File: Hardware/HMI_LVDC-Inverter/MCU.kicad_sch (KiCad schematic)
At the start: 44 parts, among them J1 UART, J9 INV, SW10 SW_MEC_5E, SW12 SW_MEC_5E, U3 ESP32-WROOM-32E, Y1 32.768KHz

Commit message: Cambios en los periféricos previo al viaje para poder seguir trabajándolo
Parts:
- renumbered SW12 to SW10, SW10 to SW9
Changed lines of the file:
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@@
 		(on_board yes)
 		(dnp no)
-		(property "Reference" "SW12"
+		(property "Reference" "SW10"
 			(at 190.246 151.13 90)
 			(effects
@@
 			(project "HMI_LVDC-Inverter"
 				(path "/0057333c-5edf-4047-9690-4d1b87a98977/a762a5f7-801c-41ef-9dab-35eab0968df2"
-					(reference "SW12")
+					(reference "SW10")
 					(unit 1)
 				)
@@
 		(on_board yes)
 		(dnp no)
-		(property "Reference" "SW10"
+		(property "Reference" "SW9"
 			(at 190.246 93.98 90)
 			(effects
@@
 			(project "HMI_LVDC-Inverter"
 				(path "/0057333c-5edf-4047-9690-4d1b87a98977/a762a5f7-801c-41ef-9dab-35eab0968df2"
-					(reference "SW10")
+					(reference "SW9")
 					(unit 1)
 				)

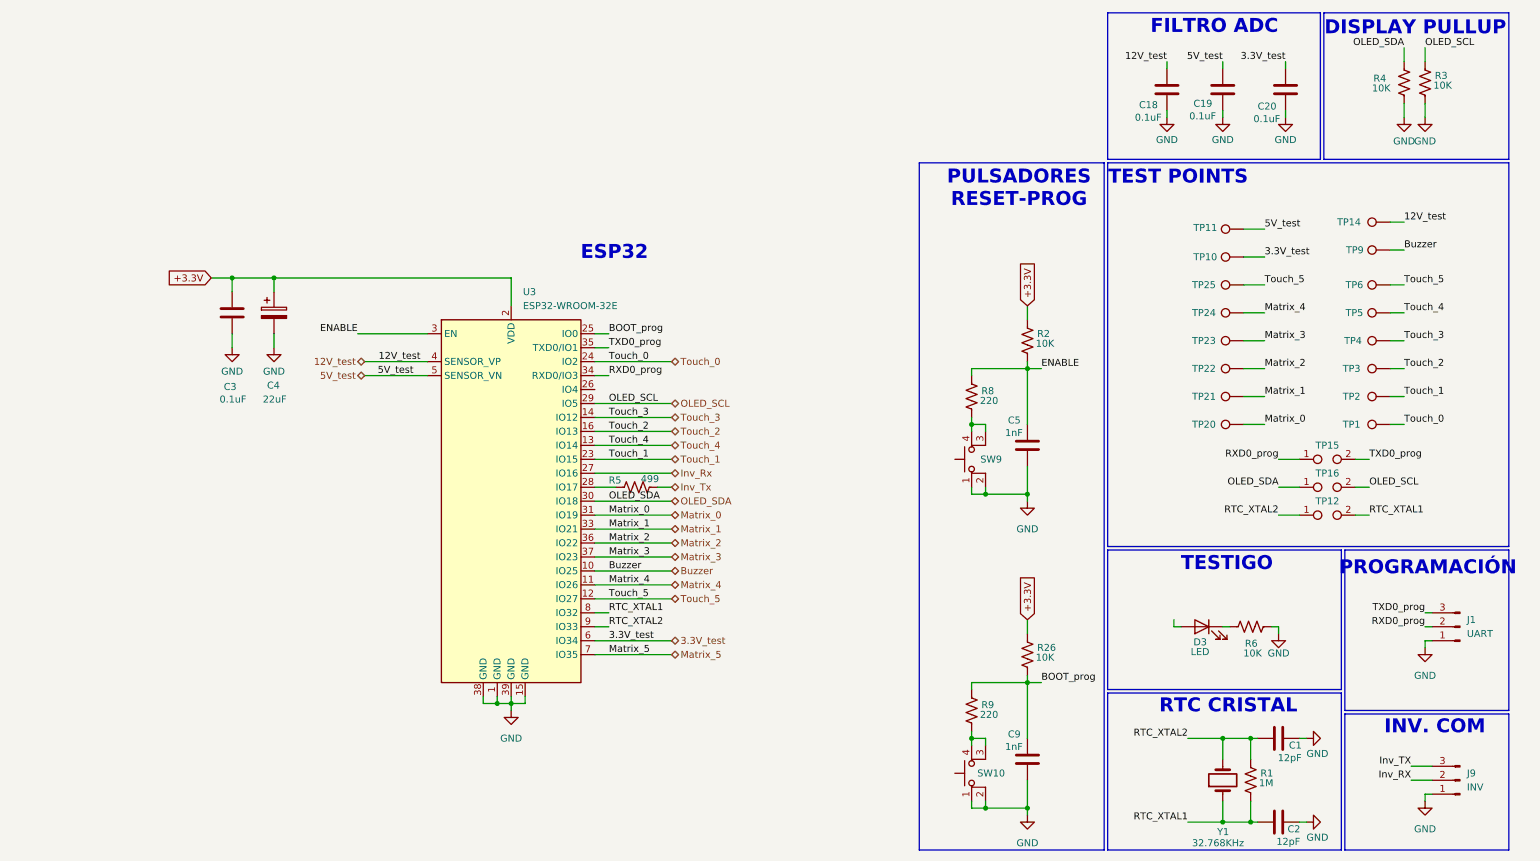
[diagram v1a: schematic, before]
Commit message: Termino de hacer las simulaciones de los periféricos. Completo los valores de componentes en esquemáticos
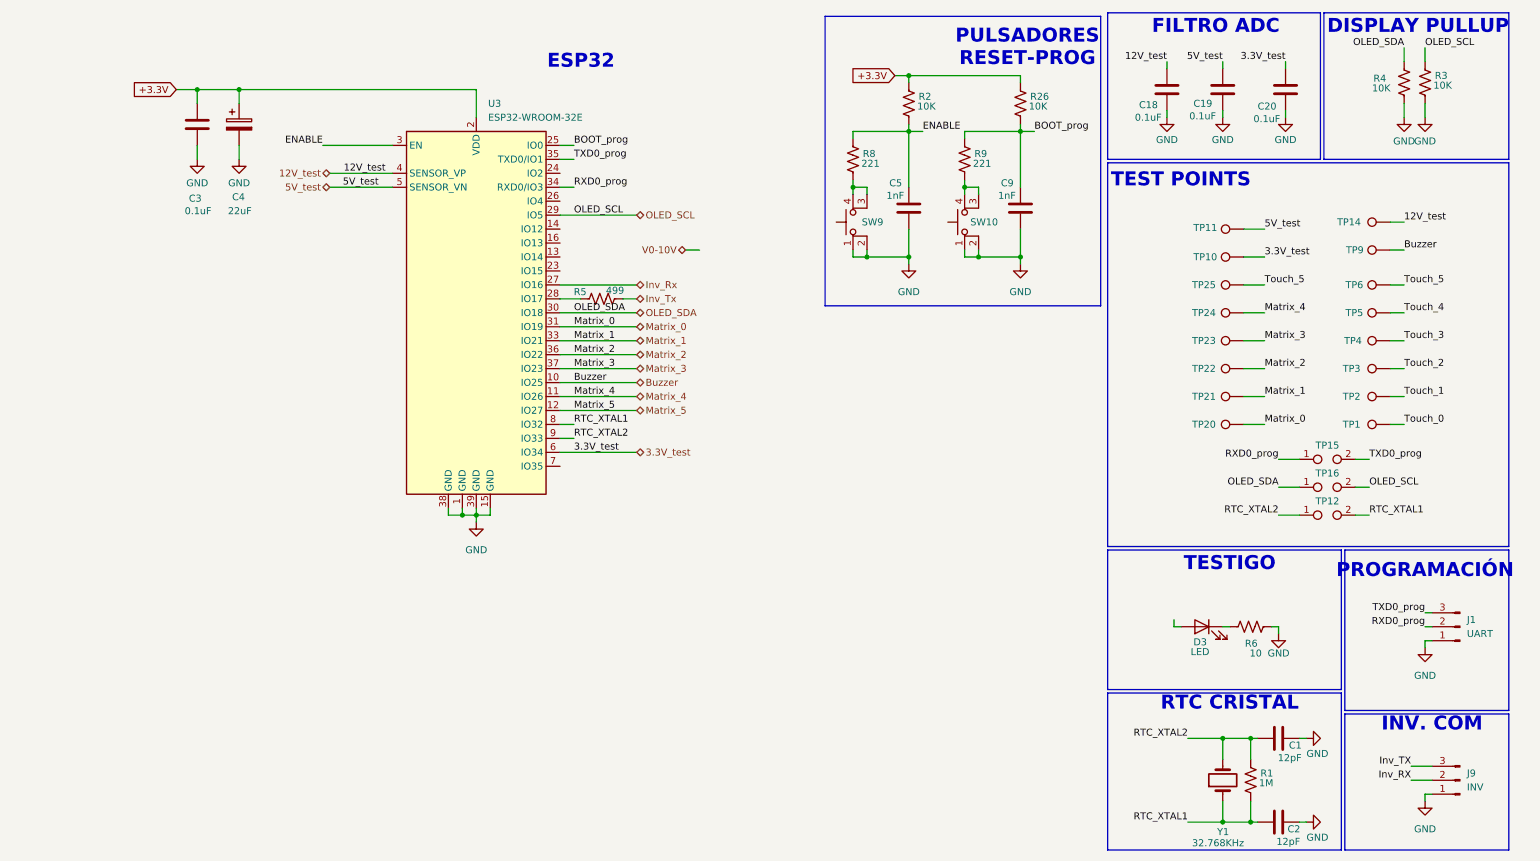
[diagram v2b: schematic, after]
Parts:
- C4: footprint Inductor_SMD:L_1206_3216Metric -> Capacitor_SMD:C_1206_3216Metric
- R6: value 10K -> 10
- R8, R9: value 220 -> 221
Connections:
- net Matrix_5: now also U3.12 (IO27); no longer U3.7 (IO35)
- net Touch_0: no longer U3.24 (IO2)
- net Touch_1: no longer U3.23 (IO15)
- net Touch_2: no longer U3.16 (IO13)
- net Touch_3: no longer U3.14 (IO12)
- net Touch_4: no longer U3.13 (IO14)
- net Touch_5: no longer U3.12 (IO27)
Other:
- moved on the sheet: C3, C4, C5, C9, R2, R26, R5, R8, R9, SW10, SW9, U3

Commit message: Terminado el esquemático del HMI
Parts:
- removed C18: 0.1uF, Capacitor_SMD:C_0603_1608Metric, symbol Device:C
- removed J1: UART, Connector_PinHeader_2.54mm:PinHeader_1x03_P2.54mm_Vertical_SMD_Pin1Left, symbol Connector:Conn_01x03_Pin
- removed J9: INV, Connector_PinHeader_2.54mm:PinHeader_1x03_P2.54mm_Vertical_SMD_Pin1Left, symbol Connector:Conn_01x03_Pin
- removed R5: 499, symbol Device:R_US
- R6: value 10 -> 102
- R8, R9, SW10, SW9: now not fitted
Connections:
- net 3.3V_test: now also U3.4 (SENSOR_VP); no longer TP10.1, U3.6 (IO34)
- net 5V_test: no longer TP11.1
- net Buzzer: no longer TP9.1
- net Matrix_0: no longer TP20.1
- net Matrix_1: no longer TP21.1
- net Matrix_2: no longer TP22.1
- net Matrix_3: no longer TP23.1
- net Matrix_4: no longer TP24.1
- net 12V_test: no longer names the net of TP14.1
- net 12V_test: no longer U3.4 (SENSOR_VP)
- net BOOT_prog renamed ESP_PROG
- net ENABLE renamed ESP_EN
- net Inv_Rx: no longer names the net of U3.27 (IO16)
- net Touch_0: no longer names the net of TP1.1
- net Touch_1: no longer names the net of TP2.1
- net Touch_2: no longer names the net of TP3.1
- net Touch_3: no longer names the net of TP4.1
- net Touch_4: no longer names the net of TP5.1
- net Touch_5: no longer names the net of TP6.1
- net Touch_5: no longer TP25.1
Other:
- note removed: "INV. COM"
- note removed: "PROGRAMACIÓN"
- moved on the sheet: C1, C19, C2, C20, C3, C4, C5, C9, D3, R1, R2, R26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

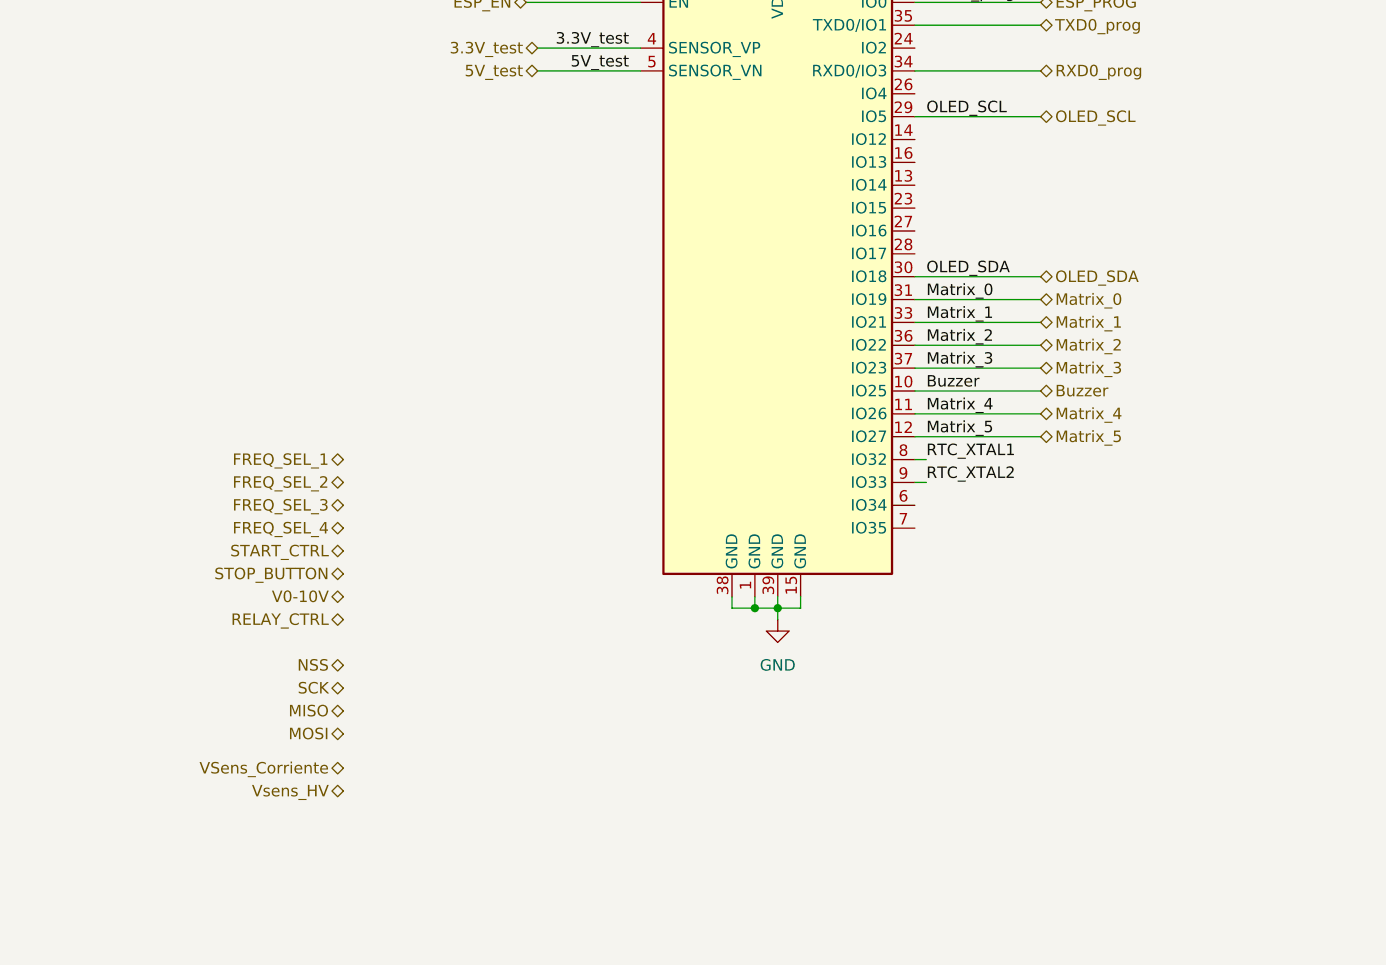
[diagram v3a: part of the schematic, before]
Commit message: Avance con el esquemático, faltan definir algunas etiquetas que no las encontré
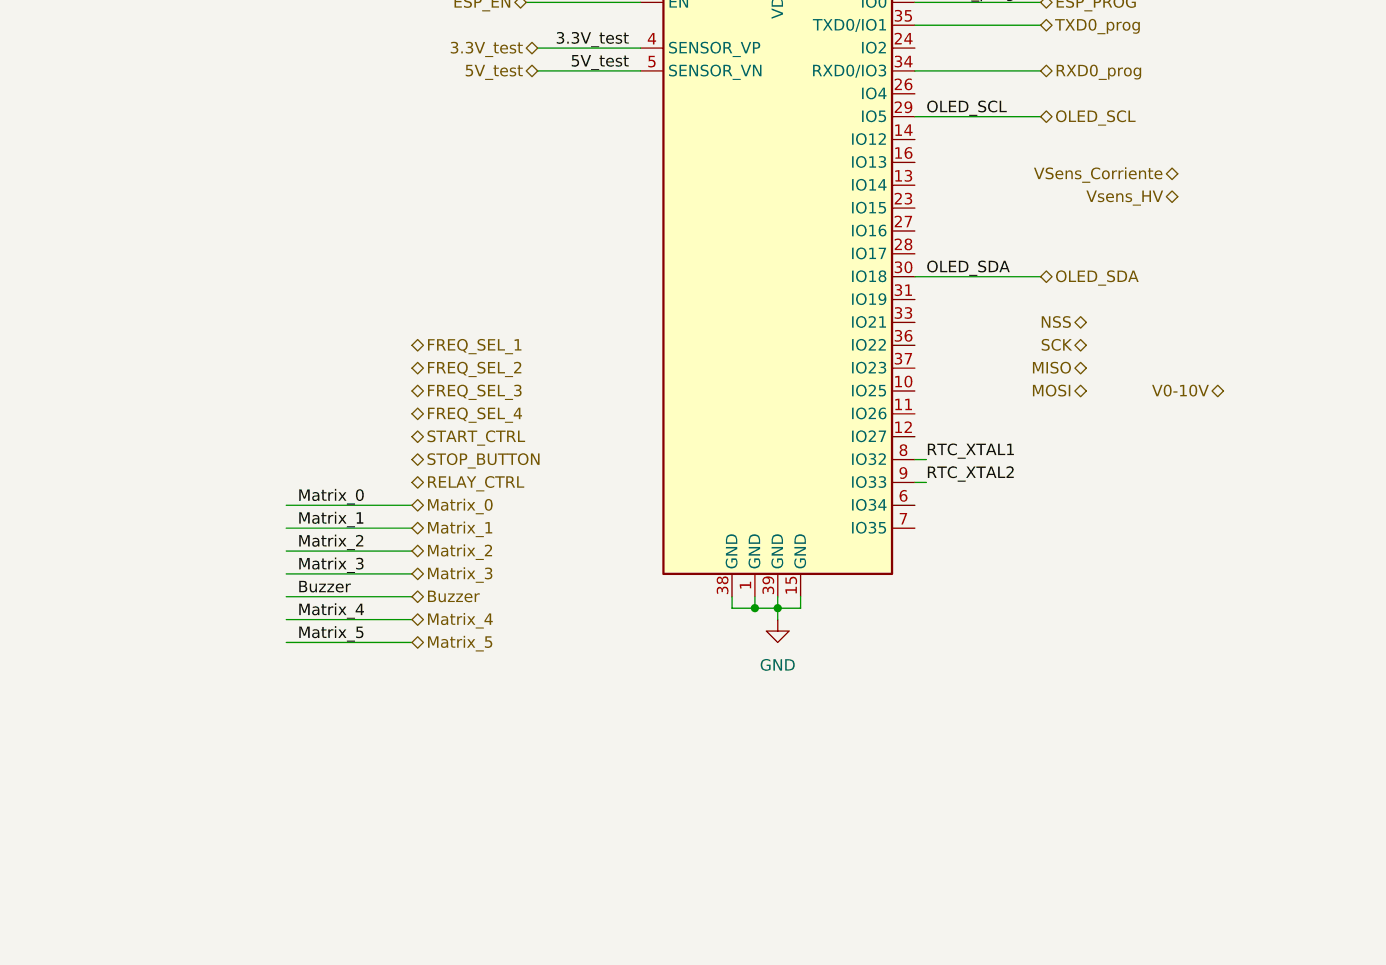
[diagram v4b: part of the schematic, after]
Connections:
- net Buzzer: no longer U3.10 (IO25)
- net Matrix_0: no longer U3.31 (IO19)
- net Matrix_1: no longer U3.33 (IO21)
- net Matrix_2: no longer U3.36 (IO22)
- net Matrix_3: no longer U3.37 (IO23)
- net Matrix_4: no longer U3.11 (IO26)
- net Matrix_5: no longer U3.12 (IO27)
